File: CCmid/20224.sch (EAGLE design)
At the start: 10 parts, among them J1 PST1,0/2-3,5, J2 PST1,0/2-3,5, U3 A6

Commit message: CCmid: referance values
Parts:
- renumbered C13 to C1, C9 to C2, D3 to D2, U3 to U1
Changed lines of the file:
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@@
 <parts>
 <part name="FRAME1" library="H-Frames" deviceset="AL" device=""/>
-<part name="U3" library="U-Linear" deviceset="AL8805" device="" value="A6"/>
+<part name="U1" library="U-Linear" deviceset="AL8805" device="" value="A6"/>
 <part name="L1" library="L-PWR" deviceset="L" device="2424" value="33uH"/>
-<part name="D3" library="D-SBR" deviceset="D" device="SMA" value="SQ4"/>
-<part name="C9" library="C-C" deviceset="C" device="C0805A" value="1uF"/>
+<part name="D2" library="D-SBR" deviceset="D" device="SMA" value="SQ4"/>
+<part name="C2" library="C-C" deviceset="C" device="C0805A" value="1uF"/>
 <part name="R1" library="R-C" deviceset="R" device="1210" value="0.30"/>
 <part name="GND5" library="Plane" deviceset="0V" device=""/>
 <part name="GND7" library="Plane" deviceset="0V" device=""/>
 <part name="R2" library="R-C" deviceset="R" device="0805" value="3.74k"/>
-<part name="C13" library="C-C" deviceset="C" device="C0805A" value="1uF"/>
+<part name="C1" library="C-C" deviceset="C" device="C0805A" value="1uF"/>
 <part name="J2" library="J-HDR3.5mm" deviceset="MCV2" device="" value="PST1,0/2-3,5"/>
 <part name="J1" library="J-HDR3.5mm" deviceset="MCV2" device="" value="PST1,0/2-3,5"/>
@@
 <instance part="FRAME1" gate="G$2" x="106.68" y="5.08"/>
 <instance part="FRAME1" gate="G$6" x="187.96" y="58.42"/>
-<instance part="U3" gate="G$1" x="129.54" y="121.92"/>
+<instance part="U1" gate="G$1" x="129.54" y="121.92"/>
 <instance part="L1" gate="G$1" x="134.62" y="137.16"/>
-<instance part="D3" gate="G$1" x="134.62" y="109.22" rot="R270"/>
-<instance part="C9" gate="G$1" x="121.92" y="137.16" rot="R90"/>
+<instance part="D2" gate="G$1" x="134.62" y="109.22" rot="R270"/>
+<instance part="C2" gate="G$1" x="121.92" y="137.16" rot="R90"/>
 <instance part="R1" gate="G$1" x="116.84" y="121.92" rot="R270"/>
 <instance part="GND5" gate="1" x="104.14" y="109.22"/>
 <instance part="GND7" gate="1" x="149.86" y="109.22"/>
 <instance part="R2" gate="G$1" x="149.86" y="119.38" rot="R90"/>
-<instance part="C13" gate="G$1" x="104.14" y="116.84"/>
+<instance part="C1" gate="G$1" x="104.14" y="116.84"/>
 <instance part="J2" gate=".1" x="81.28" y="121.92" rot="R180"/>
 <instance part="J2" gate=".2" x="81.28" y="111.76" rot="R180"/>
@@
 <wire x1="144.78" y1="111.76" x2="144.78" y2="121.92" width="0.1524" layer="91"/>
 <wire x1="144.78" y1="121.92" x2="139.7" y2="121.92" width="0.1524" layer="91"/>
-<pinref part="U3" gate="G$1" pin="GND"/>
+<pinref part="U1" gate="G$1" pin="GND"/>
 <pinref part="GND5" gate="1" pin="0V"/>
 <wire x1="144.78" y1="111.76" x2="104.14" y2="111.76" width="0.1524" layer="91"/>
-<pinref part="C13" gate="G$1" pin="2"/>
+<pinref part="C1" gate="G$1" pin="2"/>
 <junction x="104.14" y="111.76"/>
 <wire x1="83.82" y1="111.76" x2="104.14" y2="111.76" width="0.1524" layer="91"/>
@@
 <wire x1="111.76" y1="121.92" x2="111.76" y2="116.84" width="0.1524" layer="91"/>
 <wire x1="111.76" y1="116.84" x2="116.84" y2="116.84" width="0.1524" layer="91"/>
-<pinref part="U3" gate="G$1" pin="VIN"/>
+<pinref part="U1" gate="G$1" pin="VIN"/>
 <wire x1="119.38" y1="116.84" x2="116.84" y2="116.84" width="0.1524" layer="91"/>
 <junction x="116.84" y="116.84"/>
-<pinref part="D3" gate="G$1" pin="K"/>
+<pinref part="D2" gate="G$1" pin="K"/>
 <wire x1="132.08" y1="109.22" x2="116.84" y2="109.22" width="0.1524" layer="91"/>
 <wire x1="116.84" y1="109.22" x2="116.84" y2="116.84" width="0.1524" layer="91"/>
@@
 <wire x1="104.14" y1="119.38" x2="104.14" y2="121.92" width="0.1524" layer="91"/>
 <junction x="104.14" y="121.92"/>
-<pinref part="C13" gate="G$1" pin="1"/>
+<pinref part="C1" gate="G$1" pin="1"/>
 <wire x1="104.14" y1="121.92" x2="83.82" y2="121.92" width="0.1524" layer="91"/>
 <label x="92.456" y="122.936" size="1.27" layer="91"/>
@@
 <net name="IO3" class="0">
 <segment>
-<pinref part="U3" gate="G$1" pin="CTRL"/>
+<pinref part="U1" gate="G$1" pin="CTRL"/>
 <wire x1="139.7" y1="127" x2="149.86" y2="127" width="0.1524" layer="91"/>
 <pinref part="R2" gate="G$1" pin="2"/>
@@
 <net name="+CH" class="0">
 <segment>
-<pinref part="U3" gate="G$1" pin="SET"/>
+<pinref part="U1" gate="G$1" pin="SET"/>
 <pinref part="R1" gate="G$1" pin="1"/>
 <wire x1="119.38" y1="127" x2="116.84" y2="127" width="0.1524" layer="91"/>
 <wire x1="116.84" y1="127" x2="116.84" y2="137.16" width="0.1524" layer="91"/>
 <junction x="116.84" y="127"/>
-<pinref part="C9" gate="G$1" pin="1"/>
+<pinref part="C2" gate="G$1" pin="1"/>
 <wire x1="116.84" y1="137.16" x2="119.38" y2="137.16" width="0.1524" layer="91"/>
 <junction x="116.84" y="137.16"/>
@@
 <net name="-CH" class="0">
 <segment>
-<pinref part="C9" gate="G$1" pin="2"/>
+<pinref part="C2" gate="G$1" pin="2"/>
 <pinref part="L1" gate="G$1" pin="1"/>
 <wire x1="127" y1="137.16" x2="129.54" y2="137.16" width="0.1524" layer="91"/>
@@
 <net name="N$3" class="0">
 <segment>
-<pinref part="U3" gate="G$1" pin="SW"/>
+<pinref part="U1" gate="G$1" pin="SW"/>
 <wire x1="139.7" y1="116.84" x2="142.24" y2="116.84" width="0.1524" layer="91"/>
 <wire x1="142.24" y1="116.84" x2="142.24" y2="137.16" width="0.1524" layer="91"/>
@@
 <wire x1="142.24" y1="116.84" x2="142.24" y2="109.22" width="0.1524" layer="91"/>
 <junction x="142.24" y="116.84"/>
-<pinref part="D3" gate="G$1" pin="A"/>
+<pinref part="D2" gate="G$1" pin="A"/>
 <wire x1="142.24" y1="109.22" x2="137.16" y2="109.22" width="0.1524" layer="91"/>
 </segment>

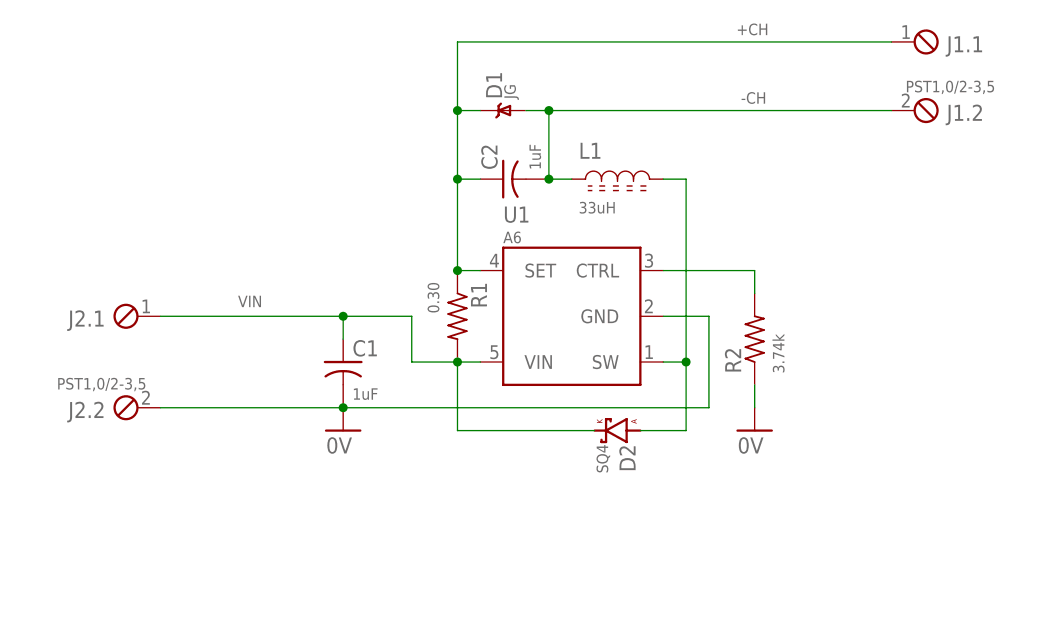
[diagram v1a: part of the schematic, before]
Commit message: CCmid: ic is obsolete
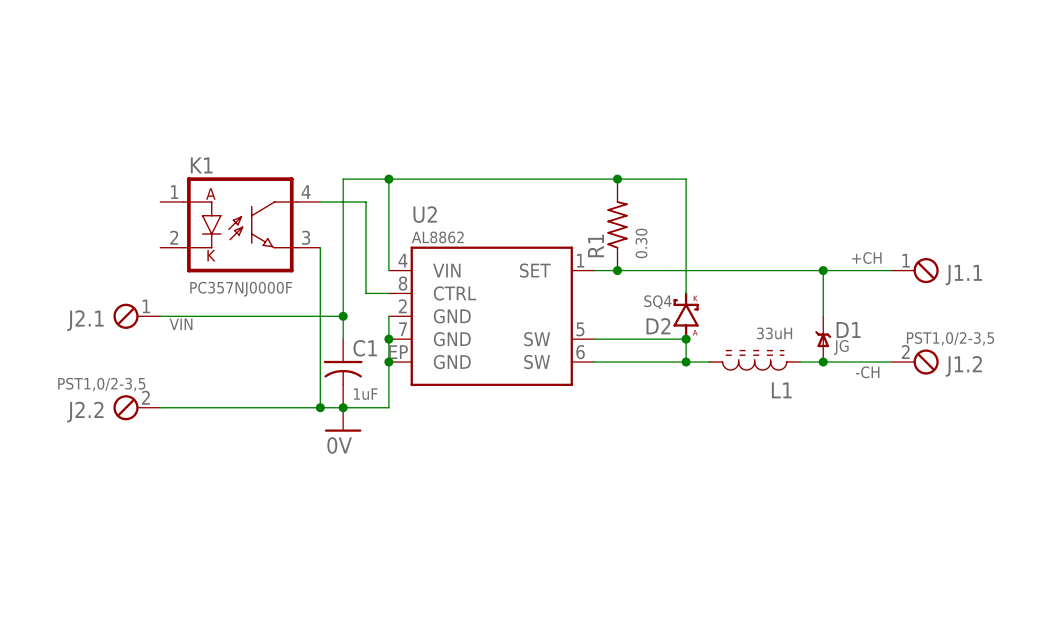
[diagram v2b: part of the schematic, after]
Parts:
- removed C2: 1uF, C-C:CC0805A
- removed R2: 3.74k, R-C:R0805
- removed U1: A6, U-Linear:AL8805
- added K1: PC357NJ0000F, K-OPT:FODM121SMD4
- added U2: AL8862, U-LED:AL8862SP-13
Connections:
- removed net IO3: R2.2, U1.CTRL
- new net N$1: K1.C, U2.CTRL
- net +CH: now also U2.SET; no longer C2.1, U1.SET
- net -CH: no longer C2.2
- net 0V: now also K1.E, U2.GND@1, U2.GND@2, U2.GND@3; no longer R2.1, U1.GND
- net N$3: now also U2.SW@1, U2.SW@2; no longer U1.SW
- net VIN: now also U2.VIN; no longer U1.VIN
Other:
- note added: "TVS"
- note added: "[KYOCERA,009296002202906] 2POS POKE-IN"
- note added: "[KYOCERA,009296004202906] 4POS POKE-IN"
- moved on the sheet: D1, D2, J1.1, J1.2, L1, R1

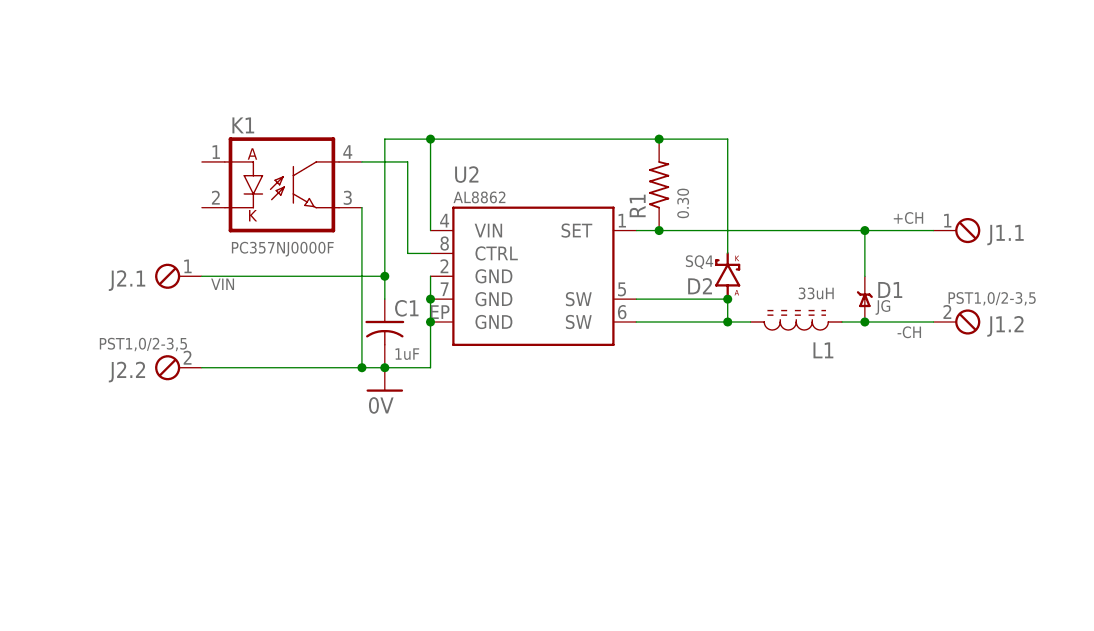
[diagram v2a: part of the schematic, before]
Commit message: CCmid: fix obsolete part, set up for bat chrg
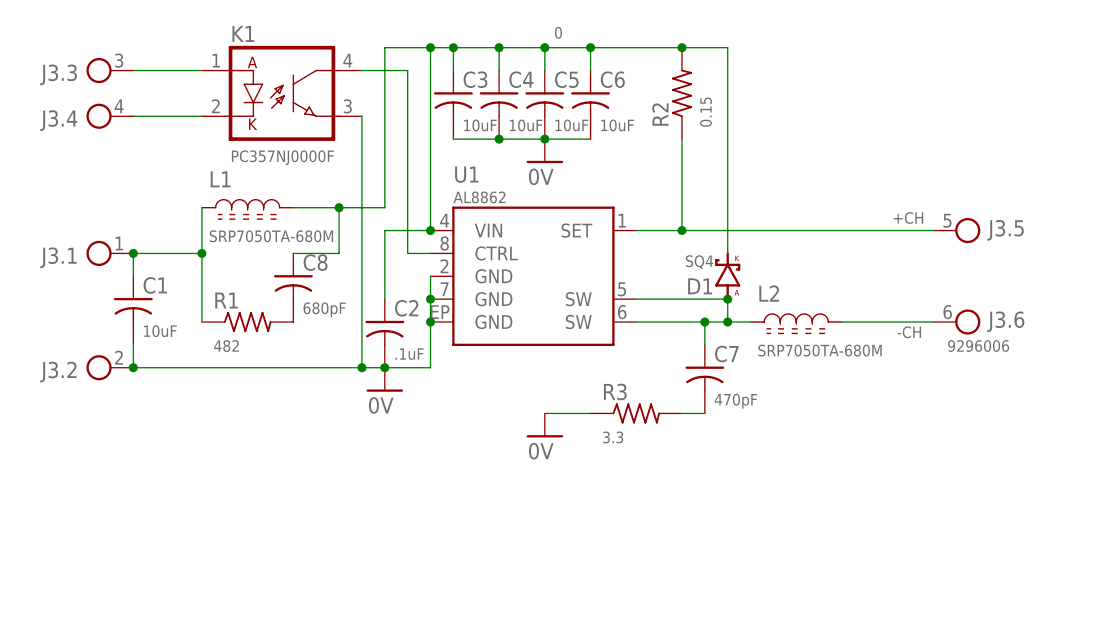
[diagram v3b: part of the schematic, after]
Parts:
- removed D2: SQ4, D-SBR:DSMA
- removed J1, J2: PST1,0/2-3,5, J-HDR3.5mm:MCV2
- added C2: .1uF, C-C:CC0805A
- added C3, C4, C5, C6: 10uF, C-C:CC1206
- added C7: 470pF, C-C:CC0603A
- added C8: 680pF, C-C:CC0603A
- added J3: 9296006, J-PokeIn:9296006
- added L2: SRP7050TA-680M, L-PWR:L2626
- added R2: 0.15, R-C:R1210
- added R3: 3.3, R-C:R0805
- C1: value 1uF -> 10uF; device C-C:CC0805A -> C-C:CC1206
- D1: value JG -> SQ4; device D-TVS:TVSSMA -> D-SBR:DSMA
- L1: value 33uH -> SRP7050TA-680M; device L-PWR:L2424 -> L-PWR:L2626
- R1: value 0.30 -> 482; device R-C:R1210 -> R-C:R0805
- renumbered U2 to U1
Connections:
- removed net VIN: C1.1, D2.K, J2.1.1, R1.2, U1.VIN
- new net 0: C2.1, C3.1, C4.1, C5.1, C6.1, C8.1, D1.K, L1.2, R2.2, U1.VIN
- new net N$2: J3.3.1, K1.A
- new net N$4: J3.4.1, K1.K
- new net N$5: C1.1, J3.1.1, L1.1, R1.1
- new net N$6: C7.2, R3.2
- new net N$7: C8.2, R1.2
- net +CH: now also J3.5.1, R2.1; no longer D1.C, J1.1.1, R1.1
- net -CH: now also J3.6.1, L2.2; no longer D1.A, J1.2.1, L1.1
- net 0V: now also C2.2, C3.2, C4.2, C5.2, C6.2, J3.2.1, R3.1; no longer J2.2.1
- net N$3: now also C7.1, D1.A, L2.1; no longer D2.A, L1.2
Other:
- note added: "670mA"
- note added: "A self-resonance notch can hold onto energy and couple it to free space (377 Ohm), so it is better to impedance match and burn off as much as possible. The notch impedance is 482 Ohm."
- note added: "A snubber is used to burn off power in parasitic LC elements that cause ringing and undesired emissions. see: https://fscdn.rohm.com/en/products/databook... /applinote/ic/power/switching_regulator... /buck_snubber_app-e.pdf"
- note added: "BAT"
- note added: "Diversion Load"
- note added: "ON/OFF"
- note added: "Use 1 to 20mA to turn off or for dimming (see PWM board)."
- note removed: "330mA"
- note removed: "TVS"
- note removed: "[KYOCERA,009296002202906] 2POS POKE-IN"
- note removed: "[KYOCERA,009296004202906] 4POS POKE-IN"
- moved on the sheet: C1, K1, L1, R1

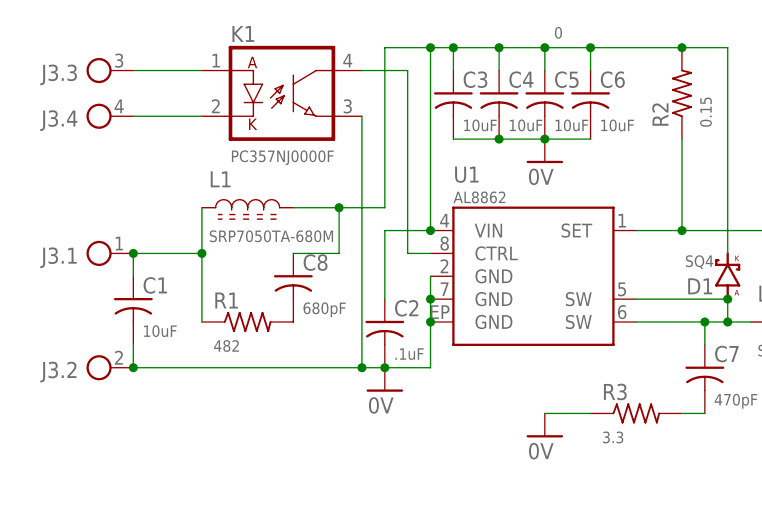
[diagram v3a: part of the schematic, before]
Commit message: CCmid: rm facing 10uF, add tvs, check inrush
that bulk voltage peak is a problem when I use the inductor to limit inrush
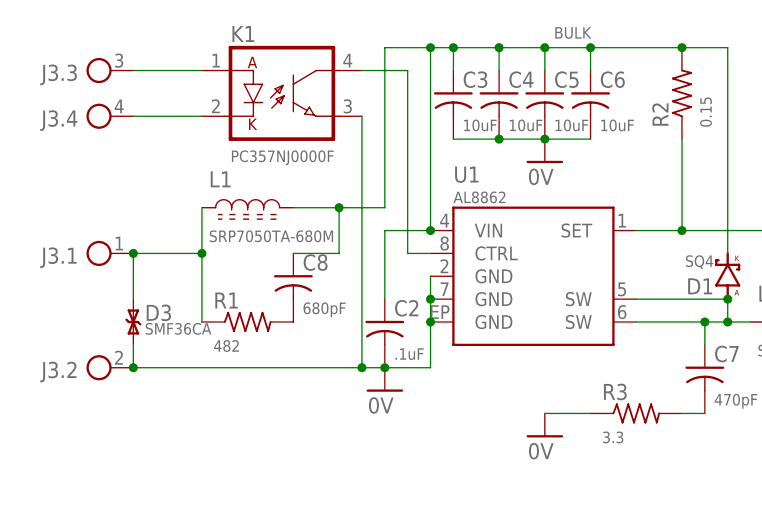
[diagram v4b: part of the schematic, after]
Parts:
- removed C1: 10uF, C-C:CC1206
- added D3: SMF36CA, D-TVS:TVS-BISOD123
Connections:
- net 0 renamed BULK
- net 0V: now also D3.A; no longer C1.2
- net N$5: now also D3.C; no longer C1.1
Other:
- note added: "30A inrush @36V on VIN."
- note added: "A 58V peak lags inrush @36V on VIN."
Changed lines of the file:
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@@
 <part name="C5" library="C-C" deviceset="C" device="C1206" value="10uF"/>
 <part name="C6" library="C-C" deviceset="C" device="C1206" value="10uF"/>
-<part name="C1" library="C-C" deviceset="C" device="C1206" value="10uF"/>
 <part name="GND1" library="Plane" deviceset="0V" device=""/>
 <part name="C7" library="C-C" deviceset="C" device="C0603A" value="470pF"/>
@@
 <part name="C8" library="C-C" deviceset="C" device="C0603A" value="680pF"/>
 <part name="R1" library="R-C" deviceset="R" device="0805" value="482"/>
+<part name="D3" library="D-TVS" deviceset="TVS-BI" device="SOD123" value="SMF36CA"/>
 </parts>
 <sheets>
@@
 impedance match and burn off as much as possible.
 The notch impedance is 482 Ohm.</text>
+<text x="61.468" y="129.794" size="1.778" layer="98">30A inrush @36V
+on VIN.</text>
+<text x="111.76" y="152.4" size="1.778" layer="98">A 58V peak lags inrush @36V on VIN.</text>
 </plain>
 <instances>
@@
 <instance part="C5" gate="G$1" x="121.92" y="142.24"/>
 <instance part="C6" gate="G$1" x="127" y="142.24"/>
-<instance part="C1" gate="G$1" x="76.2" y="119.38"/>
 <instance part="GND1" gate="1" x="121.92" y="134.62"/>
 <instance part="C7" gate="G$1" x="139.7" y="111.76"/>
@@
 <instance part="C8" gate="G$1" x="93.98" y="121.92"/>
 <instance part="R1" gate="G$1" x="88.9" y="116.84"/>
+<instance part="D3" gate="G$1" x="76.2" y="116.84"/>
 </instances>
 <busses>
@@
 <junction x="101.6" y="111.76"/>
 <pinref part="J3" gate=".2" pin="1"/>
-<pinref part="C1" gate="G$1" pin="2"/>
 <wire x1="76.2" y1="114.3" x2="76.2" y2="111.76" width="0.1524" layer="91"/>
 <junction x="76.2" y="111.76"/>
+<pinref part="D3" gate="G$1" pin="A"/>
 </segment>
 <segment>
@@
 </segment>
 </net>
-<net name="0" class="0">
+<net name="BULK" class="0">
 <segment>
 <pinref part="R2" gate="G$1" pin="2"/>
@@
 <segment>
 <pinref part="J3" gate=".1" pin="1"/>
-<pinref part="C1" gate="G$1" pin="1"/>
-<wire x1="76.2" y1="124.46" x2="76.2" y2="121.92" width="0.1524" layer="91"/>
+<wire x1="76.2" y1="124.46" x2="76.2" y2="119.38" width="0.1524" layer="91"/>
 <pinref part="L1" gate="G$1" pin="1"/>
 <junction x="76.2" y="124.46"/>
@@
 <wire x1="83.82" y1="116.84" x2="83.82" y2="124.46" width="0.1524" layer="91"/>
 <junction x="83.82" y="124.46"/>
-</segment>
-</net>
+<pinref part="D3" gate="G$1" pin="C"/>
+</segment>
+</net>
